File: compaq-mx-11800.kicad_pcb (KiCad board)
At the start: 2 copper layers, 387.1 x 166.4 mm, 246 parts

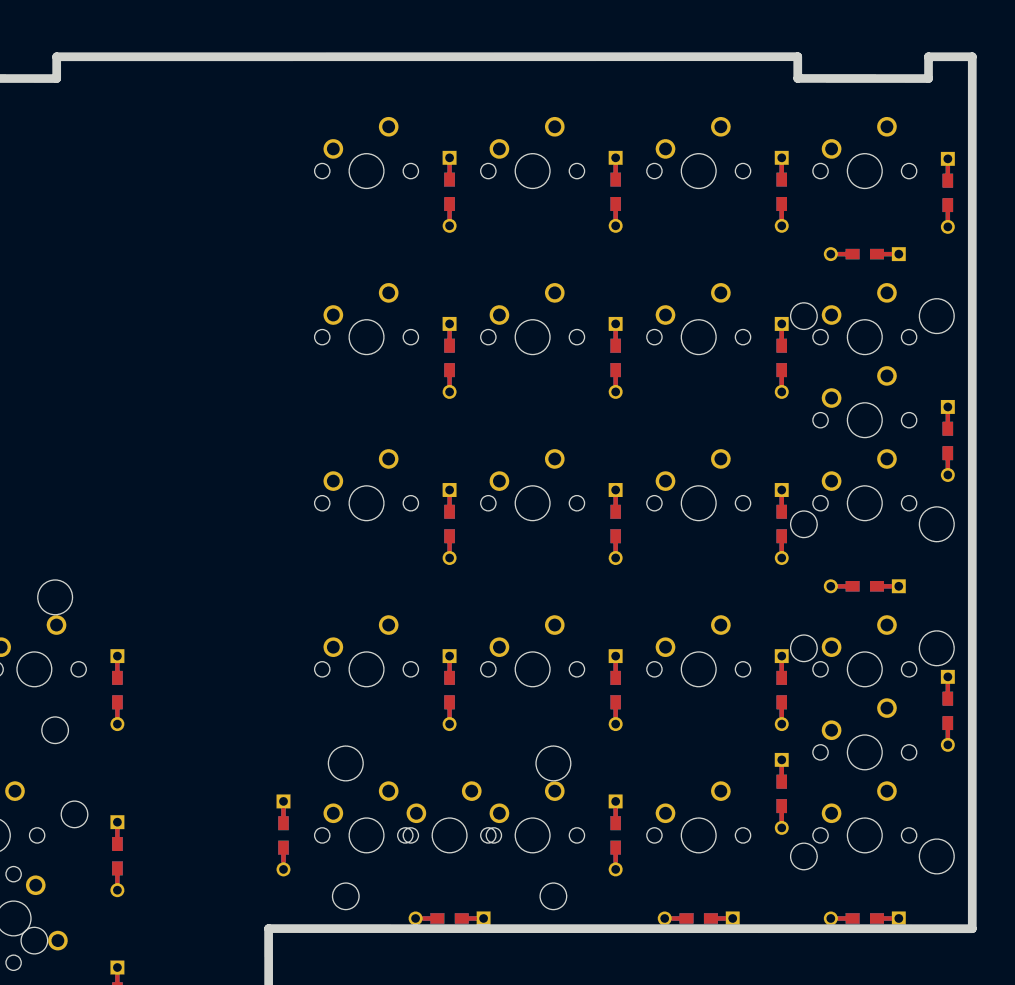
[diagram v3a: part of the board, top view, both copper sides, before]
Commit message: readjust pcb size and 2 mounting holes
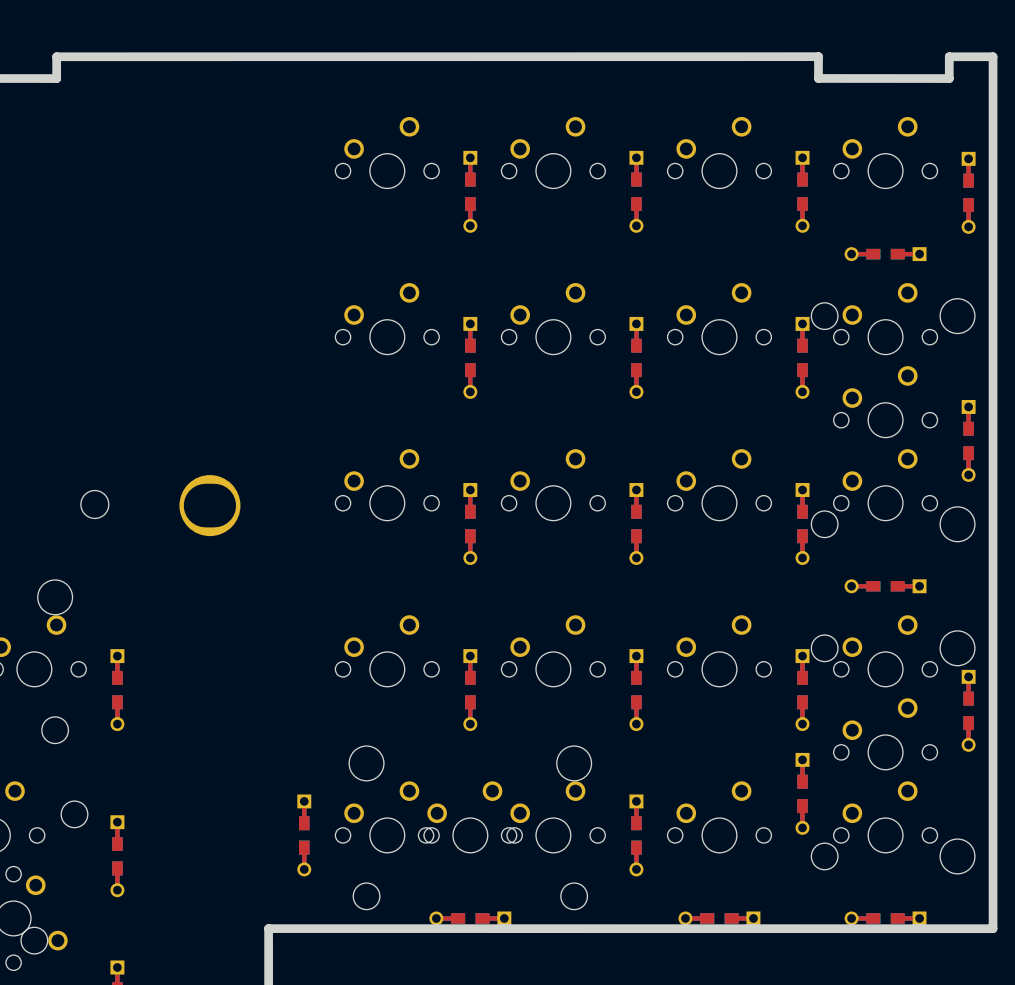
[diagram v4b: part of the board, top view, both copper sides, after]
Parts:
- added ?: MountingHole_3.2mm_M3, MountingHole:MountingHole_3.2mm_M3, F.Cu at (240.3, 97.8)
- added ?: MountingHole_2.1mm, MountingHole:MountingHole_2.1mm, F.Cu at (253.5, 97.9)
- moved D15 2.38 mm to (321.5, 61.9)
- moved D16 2.38 mm to (340.5, 62.0)
- moved D30 2.38 mm to (321.5, 81.0)
- moved D32 2.38 mm to (340.5, 90.5)
- moved D36 2.38 mm to (321.5, 100.0)
- moved D52 2.38 mm to (340.5, 121.4)
- moved D53 2.38 mm to (321.5, 131.0)
- moved D56 2.38 mm to (321.5, 119.1)
- moved D73 2.38 mm to (311.9, 145.3)
- moved D90 2.38 mm to (264.3, 135.7)
- moved MX13 2.38 mm to (273.8, 59.5)
- moved MX14 2.38 mm to (292.9, 59.5)
- moved MX15 2.38 mm to (311.9, 59.5)
- moved MX28 2.38 mm to (273.8, 78.6)
- moved MX29 2.38 mm to (292.9, 78.6)
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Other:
- board size 387.1 x 166.4 mm -> 389.5 x 166.4 mm

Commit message: add rest of the pcb mounting holes
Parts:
- removed ?: MountingHole_3.2mm_M3, MountingHole:MountingHole_3.2mm_M3
- removed ?: MountingHole_2.1mm, MountingHole:MountingHole_2.1mm
- added H1: MountingHole, MountingHole:MountingHole_3.2mm_M3, F.Cu at (-34.6, 97.3)
- added H2: MountingHole, MountingHole:MountingHole_3.2mm_M3, F.Cu at (239.0, 98.1)
- added H3: MountingHole, MountingHole:MountingHole_3.2mm_M3, F.Cu at (144.2, 97.5)
- added H4: MountingHole, MountingHole:MountingHole_3.2mm_M3, F.Cu at (252.3, 98.1)
- added H5: MountingHole, MountingHole:MountingHole_3.2mm_M3, F.Cu at (56.2, 97.9)
- added H6: MountingHole, Keebio-Parts:SolidCopper, B.Cu at (330.1, 143.2)
- moved D57 18.5 mm to (342.9, 131.1), turned to 90 degrees

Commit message: remove extra diodes for multilayout
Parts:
- removed D106, D109, D110, D111, D112, D113, D119, D17, D50, D52, D75, D89, D90: D_Small, Keebio-Parts:Diode-dual
- moved D107 22.0 mm to (209.6, 183.4), turned to 0 degrees
- moved D72 21.3 mm to (264.3, 135.7), turned to 90 degrees
- moved D92 17.3 mm to (228.6, 173.9)
- moved D122 16.8 mm to (9.53, 195.1), turned to 90 degrees
- moved D117 16.0 mm to (133.3, 195.1), turned to 90 degrees
- moved D118 13.9 mm to (178.6, 195.3), turned to 90 degrees
- moved D56 12.7 mm to (311.0, 126.2), turned to 0 degrees
- moved D53 9.41 mm to (321.5, 121.6)
- moved D120 7.49 mm to (90.5, 195.1)
- moved D57 5.43 mm to (340.5, 126.2)
- moved D12 4.76 mm to (223.8, 61.8)
- moved D31 0.98 mm to (222.9, 107.2)
- moved D124 0.24 mm to (202.4, 195.4)
- moved D73 0.12 mm to (312.1, 145.3)
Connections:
- MX106 pad 2: Net-(D106-Pad2) -> Net-(D107-Pad2)
- MX109 pad 2: Net-(D109-Pad2) -> Net-(D117-Pad2)
- MX110 pad 2: Net-(D110-Pad2) -> Net-(D118-Pad2)
- MX111 pad 2: Net-(D111-Pad2) -> Net-(D121-Pad2)
- MX112 pad 2: Net-(D112-Pad2) -> Net-(D122-Pad2)
- MX113 pad 2: Net-(D113-Pad2) -> Net-(D120-Pad2)
- MX119 pad 2: Net-(D119-Pad2) -> Net-(D124-Pad2)
- MX17 pad 2: Net-(D17-Pad2) -> Net-(D32-Pad2)
- MX50 pad 2: Net-(D50-Pad2) -> Net-(D31-Pad2)
- MX52 pad 2: Net-(D52-Pad2) -> Net-(D53-Pad2)
- MX75 pad 2: Net-(D75-Pad2) -> Net-(D76-Pad2)
- MX89 pad 2: Net-(D89-Pad2) -> Net-(D74-Pad2)
- MX90 pad 2: Net-(D90-Pad2) -> Net-(D72-Pad2)

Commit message: correct diode placement and orientation
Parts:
- D108, D114, D115, D116, D117, D118, D120, D121, D122, D124: moved to B.Cu
- moved D108 3.37 mm to (252.4, 181.0)
- moved D115 3.37 mm to (252.4, 200.0)
- moved D114 3.37 mm to (271.5, 200.0)
- moved D116 3.28 mm to (233.4, 200.0)

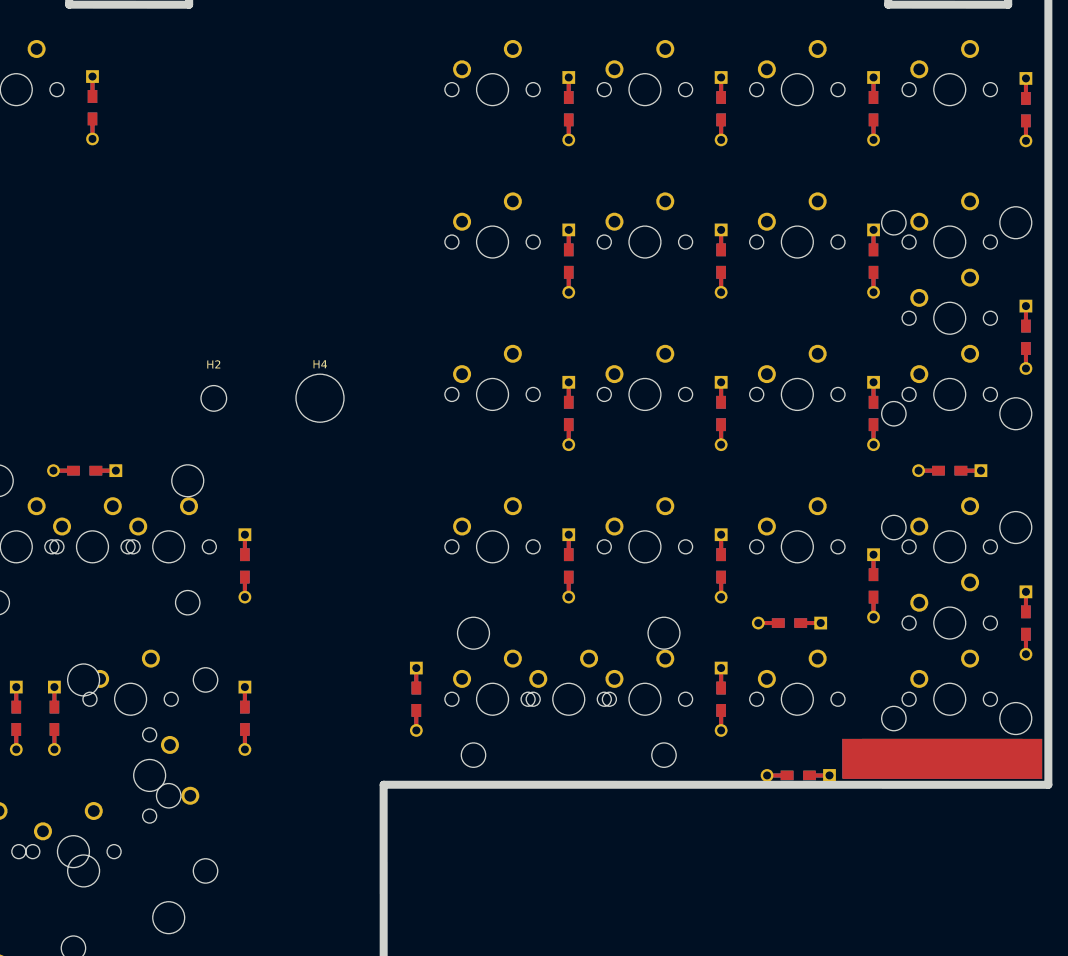
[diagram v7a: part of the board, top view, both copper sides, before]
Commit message: connect numpad diodes
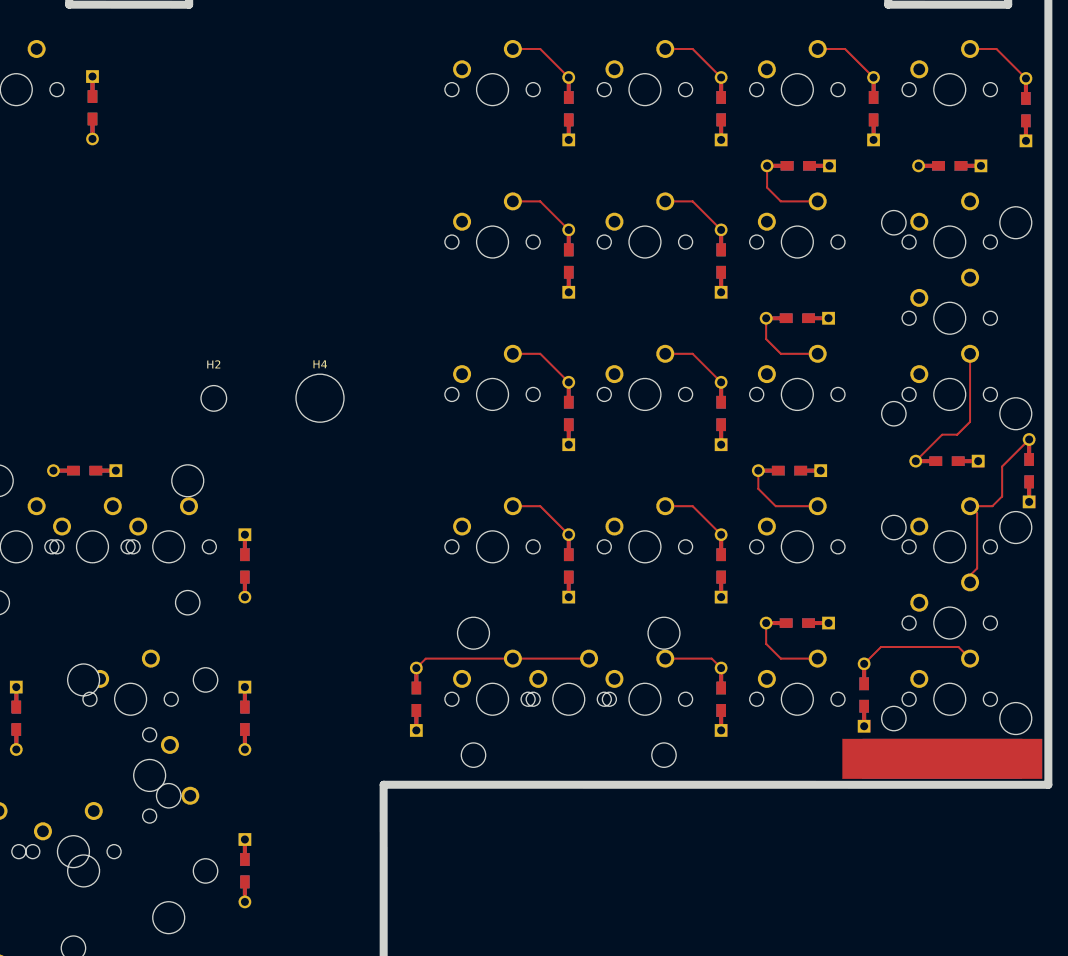
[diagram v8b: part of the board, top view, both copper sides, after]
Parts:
- moved D74 30.5 mm to (242.9, 157.2)
- moved D53 24.2 mm to (340.9, 107.2), turned to 270 degrees
- moved D32 23.5 mm to (331.0, 69.1), turned to 0 degrees
- moved D57 22.1 mm to (320.3, 135.2), turned to 270 degrees
- moved D73 19.1 mm to (311.9, 126.2)
- moved D56 19.0 mm to (311.0, 107.2)
- moved D36 15.2 mm to (311.9, 88.1), turned to 0 degrees
- moved D30 15.2 mm to (312.1, 69.1), turned to 0 degrees
- moved D33 1.24 mm to (330.6, 106.0)
- turned D13 to 270 degrees
- turned D14 to 270 degrees
- turned D15 to 270 degrees
- turned D16 to 270 degrees
- turned D28 to 270 degrees
- turned D29 to 270 degrees
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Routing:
- net Net-(D53-Pad2): track 0.00 -> 23.7 mm
- net Net-(D72-Pad2): track 0.00 -> 22.1 mm
- net Net-(D33-Pad2): track 0.00 -> 17.3 mm
- net Net-(D57-Pad2): track 0.00 -> 14.7 mm
- net Net-(D36-Pad2): track 0.00 -> 10.7 mm
- net Net-(D56-Pad2): track 0.00 -> 10.6 mm
- net Net-(D73-Pad2): track 0.00 -> 9.81 mm
- net Net-(D30-Pad2): track 0.00 -> 9.76 mm
- net Net-(D16-Pad2): track 0.00 -> 8.51 mm
- net Net-(D55-Pad2): track 0.00 -> 8.46 mm
- net Net-(D35-Pad2): track 0.00 -> 8.46 mm
- net Net-(D29-Pad2): track 0.00 -> 8.46 mm
- net Net-(D15-Pad2): track 0.00 -> 8.46 mm
- net Net-(D14-Pad2): track 0.00 -> 8.46 mm
- net Net-(D54-Pad2): track 0.00 -> 8.46 mm
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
